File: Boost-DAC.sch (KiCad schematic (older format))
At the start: 20 parts, among them Q17 BSZ100N06NSATMA1, U6 LTC3873, U7 MAX5215

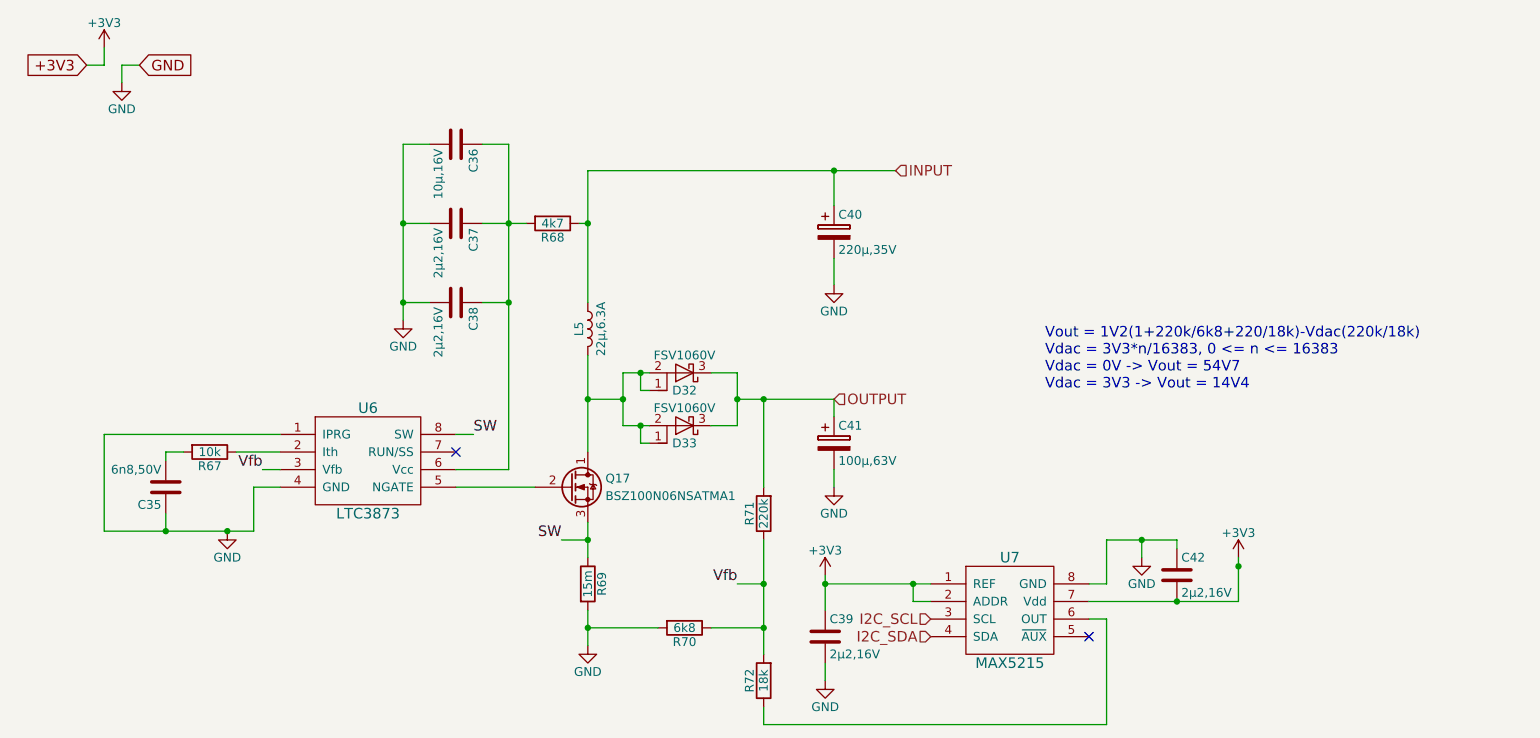
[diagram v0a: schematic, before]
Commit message: HW 0.2 finalized schematic and pcb files, BOM needs to be checked
Lots of major and little problems fixed found in the 0.1

Major changes:
-LTC6803-3 footprint changed to it's correct one
-Boost converter layout and capacitor optimization
-MCU switched from STM32F070CBT6 to ultra low power STM32L433CCT6 to improve sleep state power consumption
-Button/LED + Comms connectors switched from THT JST-XH to SMD JST-PH
-CAN-bus support added
-Changed power regulator setup for "always on"

Minor changes:
-Changed cell balance resistor sizes from 0603 to 0402 in order to get a bit more breathing room during soldering
-External oscillator removed from MCU, because new one has everything available internally
-Comms connector has USART or CAN available via solder bridges
-Sense resistors switched to higher resistance ones to lower deep sleep standby current
-etc.
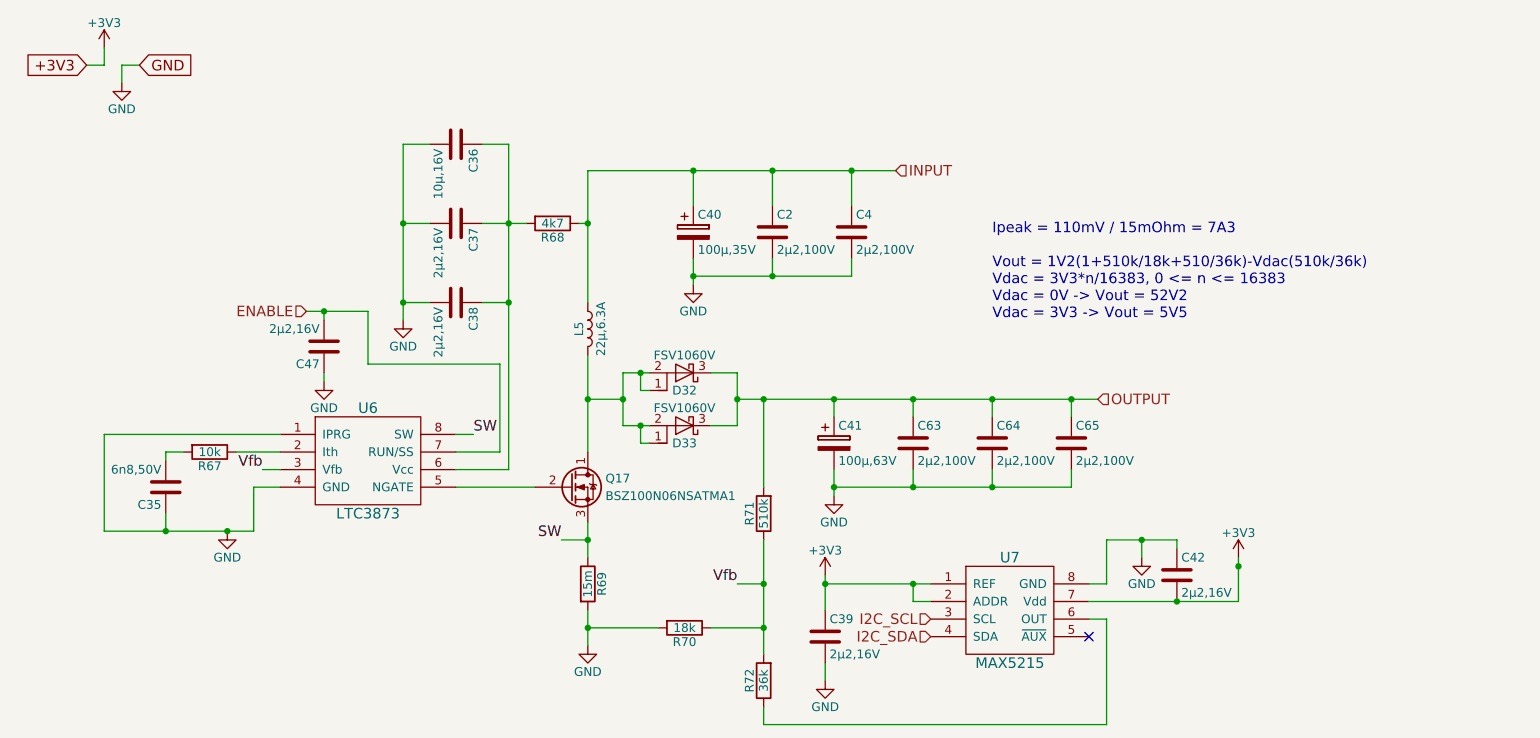
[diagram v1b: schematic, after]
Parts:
- added C2, C4, C63, C64, C65: 2µ2,100V, Capacitors_SMD:C_1210, symbol C
- added C47: 2µ2,16V, Capacitors_SMD:C_0603, symbol C
- C35: MFG GCM188R71H682KA37D -> ANY; TempCo. (none) -> X7R
- C36: MFG CC1206KKX7R7BB106 -> ANY; TempCo. (none) -> X7R
- C37, C38, C39, C42: MFG EMK107BJ225KA-T -> ANY; TempCo. (none) -> X5R
- C40: value 220µ,35V -> 100µ,35V; footprint Capacitors_SMD:CP_Elec_8x10 -> Capacitors_SMD:CP_Elec_6.3x7.7; MFG UWT1V221MNL1GS -> EEE-FPV101XAP
- C41: MFG EEE-1JA101P -> EEE-FK1J101P
- R67: MFG RC0603FR-0710KL -> ANY; Tol. (none) -> 1%
- R68: MFG RC0603FR-074K7L -> ANY; Tol. (none) -> 1%
- R69: MFG KRL1632E-M-R015-F-T5 -> ANY; Power (none) -> 0.75W; Tol. (none) -> 1%
- R70: value 6k8 -> 18k; Field4 RC0603FR-076K8L -> (none); MFG (none) -> ANY; Tol. (none) -> 1%
- R71: value 220k -> 510k; MFG RC0603FR-07220KL -> ANY; Tol. (none) -> 1%
- R72: value 18k -> 36k; MFG RC0603FR-0718KL -> ANY; Tol. (none) -> 1%
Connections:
- net GND: now also C2.2, C4.2, C47.1, C63.2, C64.2, C65.2
- net INPUT: now also C2.1, C4.1
- net OUTPUT: now also C63.1, C64.1, C65.1
- net ENABLE: now reaches U6.7 (RUN/SS)
- net ENABLE: now also C47.2
- no-connect marks 2 -> 1
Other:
- note added: "Ipeak = 110mV / 15mOhm = 7A3\n\nVout = 1V2(1+510k/18k+510/36k)-Vdac(510k/36k)\nVdac = 3V3*n/16383, 0 <= n <= 16383\nVdac = 0V -> Vout = 52V2\nVdac = 3V3 -> Vout = 5V5"
- note removed: "Vout = 1V2(1+220k/6k8+220/18k)-Vdac(220k/18k)\nVdac = 3V3*n/16383, 0 <= n <= 16383\nVdac = 0V -> Vout = 54V7\nVdac = 3V3 -> Vout = 14V4"
- moved on the sheet: C40
